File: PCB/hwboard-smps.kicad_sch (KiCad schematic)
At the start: 0 parts

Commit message: add dc dc schematic
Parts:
- added C1, C2, C3, C4, C5, C6, C7, C8: C, symbol Device:C
- added L1: L, symbol Device:L
- added R1, R2, R3, R4, R5: R, symbol Device:R
- added U2: TPS61089, Package_DFN_QFN:Texas_VQFN-RNR0011A-11, symbol Regulator_Switching:TPS61089
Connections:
- new net: R3.2, R4.1, U2.3 (FB)
- new net: R5.1, U2.8 (ILIM)
- new net: C7.1, R2.1, U2.4 (COMP)
- new net: C8.1, R2.2
- new net: C3.1, U2.2 (VCC)
- new net: C1.1, L1.2, R1.1, U2.11 (SW)
- new net: R1.2, U2.1 (FSW)
- new net: C1.2, U2.10 (BOOT)
- new net EN: U2.7 (EN)
- new net GND: C2.2, C3.2, C4.2, C5.2, C6.2, C7.2, C8.2, R4.2, R5.2, U2.5 (GND)
- new net V_{IN}: C2.1, L1.1, U2.9 (VIN)
- new net V_{OUT}: C4.1, C5.1, C6.1, R3.1, U2.6 (VOUT)

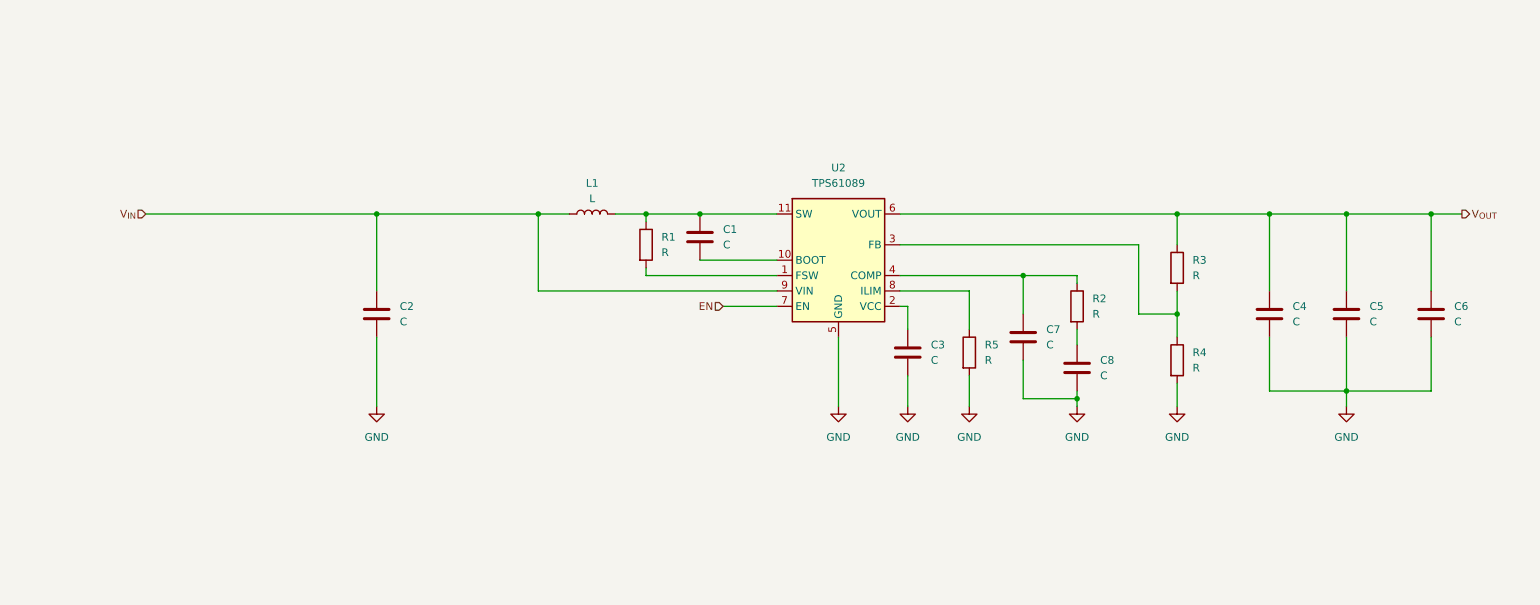
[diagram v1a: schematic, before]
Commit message: add boost components
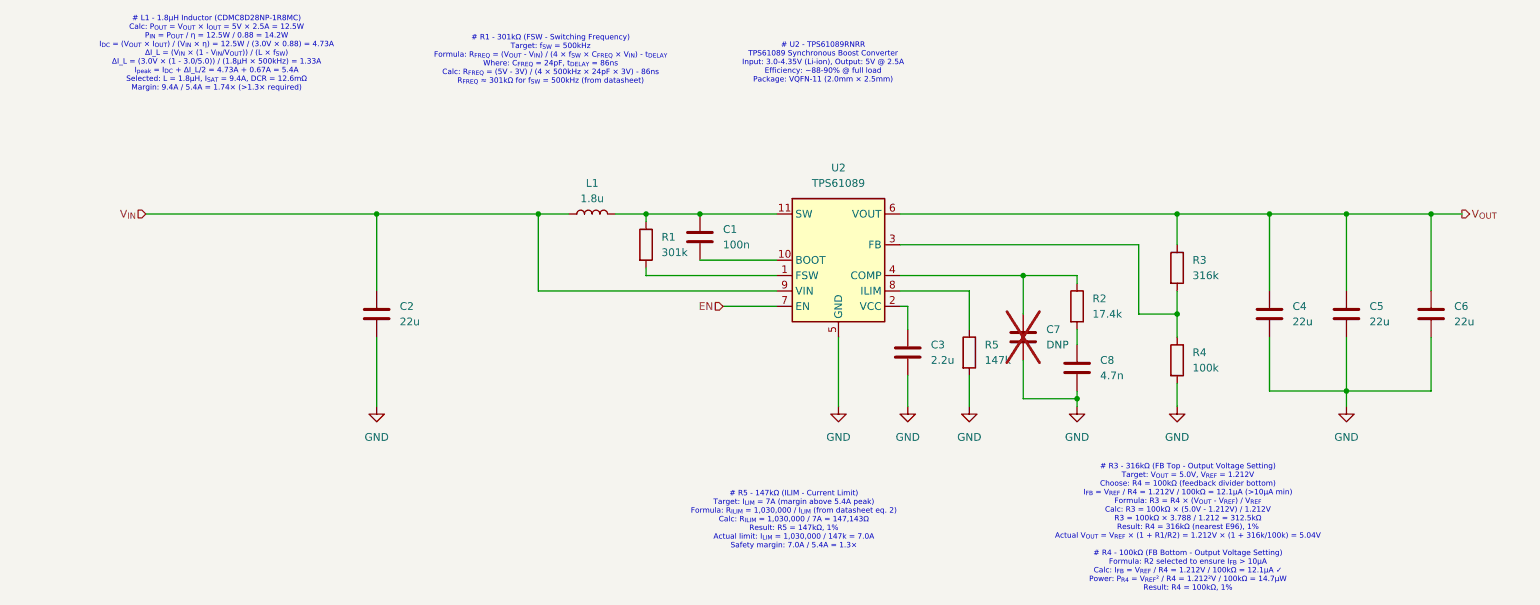
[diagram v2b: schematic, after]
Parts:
- C1: value C -> 100n
- C2, C4, C5, C6: value C -> 22u
- C3: value C -> 2.2u
- C7: value C -> DNP; now not fitted
- C8: value C -> 4.7n
- L1: value L -> 1.8u
- R1: value R -> 301k
- R2: value R -> 17.4k
- R3: value R -> 316k
- R4: value R -> 100k
- R5: value R -> 147k
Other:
- note added: "# L1 - 1.8µH Inductor (CDMC8D28NP-1R8MC) Calc: P_{OUT} = V_{OUT} × I_{OUT} = 5V × 2.5A = 12.5W P_{IN} = P_{OUT} / η = 12.5W / 0.88 = 14.2W I_{DC} = (V_{OUT} × I_{OUT}) / (V_{IN} × η) = 12.5W / (3.0V × 0.88) = 4.73A ΔI_L = (V_{IN} × (1 - V_{IN}/V_{OUT})) / (L × f_{SW}) ΔI_L = (3.0V × (1 - 3.0/5.0)) / (1.8µH × 500kHz) = 1.33A I_{peak} = I_{DC} + ΔI_L/2 = 4.73A + 0.67A = 5.4A Selected: L = 1.8µH, I_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"
- note added: "# R1 - 301kΩ (FSW - Switching Frequency) Target: f_{SW} = 500kHz Formula: R_{FREQ} = (V_{OUT} - V_{IN}) / (4 × f_{SW} × C_{FREQ} × V_{IN}) - t_{DELAY} Where: C_{FREQ} = 24pF, t_{DELAY} = 86ns Calc: R_{FREQ} = (5V - 3V) / (4 × 500kHz × 24pF × 3V) - 86ns R_{FREQ} ≈ 301kΩ for f_{SW} = 500kHz (from datasheet)"
- note added: "# R3 - 316kΩ (FB Top - Output Voltage Setting) Target: V_{OUT} = 5.0V, V_{REF} = 1.212V Choose: R4 = 100kΩ (feedback divider bottom) I_{FB} = V_{REF} / R4 = 1.212V / 100kΩ = 12.1µA (>10µA min) Formula: R3 = R4 × (V_{OUT} - V_{REF}) / V_{REF} Calc: R3 = 100kΩ × (5.0V - 1.212V) / 1.212V R3 = 100kΩ × 3.788 / 1.212 = 312.5kΩ Result: R4 = 316kΩ (nearest E96), 1% Actual V_{OUT} = V_{REF} × (1 + R1/R2) 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"
- note added: "# R5 - 147kΩ (ILIM - Current Limit) Target: I_{LIM} = 7A (margin above 5.4A peak) Formula: R_{ILIM} = 1,030,000 / I_{LIM} (from datasheet eq. 2) Calc: R_{ILIM} = 1,030,000 / 7A = 147,143Ω Result: R5 = 147kΩ, 1% Actual limit: I_{LIM} = 1,030,000 / 147k = 7.0A Safety margin: 7.0A / 5.4A = 1.3×"
- note added: "# U2 - TPS61089RNRR TPS61089 Synchronous Boost Converter Input: 3.0-4.35V (Li-ion), Output: 5V @ 2.5A Efficiency: ~88-90% @ full load Package: VQFN-11 (2.0mm × 2.5mm)"
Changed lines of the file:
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@@
 	(generator_version "9.0")
 	(paper "A4")
+	(text "# U2 - TPS61089RNRR\nTPS61089 Synchronous Boost Converter\nInput: 3.0-4.35V (Li-ion), Output: 5V @ 2.5A\nEfficiency: ~88-90% @ full load\nPackage: VQFN-11 (2.0mm × 2.5mm)"
+		(exclude_from_sim no)
+		(at 148.59 64.008 0)
+		(effects
+			(font
+				(size 0.889 0.889)
+			)
+		)
+	)
+	(text "# R5 - 147kΩ (ILIM - Current Limit)\nTarget: I_{LIM} = 7A (margin above 5.4A peak)\nFormula: R_{ILIM} = 1,030,000 / I_{LIM} (from datasheet eq. 2)\nCalc: R_{ILIM} = 1,030,000 / 7A = 147,143Ω\nResult: R5 = 147kΩ, 1%\nActual limit: I_{LIM} = 1,030,000 / 147k = 7.0A\nSafety margin: 7.0A / 5.4A = 1.3×"
+		(exclude_from_sim no)
+		(at 143.764 139.446 0)
+		(effects
+			(font
+				(size 0.889 0.889)
+			)
+		)
+	)
+	(text "# R1 - 301kΩ (FSW - Switching Frequency)\nTarget: f_{SW} = 500kHz\nFormula: R_{FREQ} = (V_{OUT} - V_{IN}) / (4 × f_{SW} × C_{FREQ} × V_{IN}) - t_{DELAY}\nWhere: C_{FREQ} = 24pF, t_{DELAY} = 86ns\nCalc: R_{FREQ} = (5V - 3V) / (4 × 500kHz × 24pF × 3V) - 86ns\nR_{FREQ} ≈ 301kΩ for f_{SW} = 500kHz (from datasheet)"
+		(exclude_from_sim no)
+		(at 103.632 63.5 0)
+		(effects
+			(font
+				(size 0.889 0.889)
+			)
+		)
+	)
+	(text "# R3 - 316kΩ (FB Top - Output Voltage Setting)\nTarget: V_{OUT} = 5.0V, V_{REF} = 1.212V\nChoose: R4 = 100kΩ (feedback divider bottom)\nI_{FB} = V_{REF} / R4 = 1.212V / 100kΩ = 12.1µA (>10µA min)\nFormula: R3 = R4 × (V_{OUT} - V_{REF}) / V_{REF}\nCalc: R3 = 100kΩ × (5.0V - 1.212V) / 1.212V\nR3 = 100kΩ × 3.788 / 1.212 = 312.5kΩ\nResult: R4 = 316kΩ (nearest E96), 1%\nActual V_{OUT} = V_{REF} × (1 + R1/R2) = 1.212V × (1 + 316k/100k) = 5.04V\n\n# R4 - 100kΩ (FB Bottom - Output Voltage Setting)\nFormula: R2 selected to ensure I_{FB} > 10µA\nCalc: I_{FB} = V_{REF} / R4 = 1.212V / 100kΩ = 12.1µA ✓\nPower: P_{R4} = V_{REF}² / R4 = 1.212²V / 100kΩ = 14.7µW\nResult: R4 = 100kΩ, 1%"
+		(exclude_from_sim no)
+		(at 208.788 140.716 0)
+		(effects
+			(font
+				(size 0.889 0.889)
+			)
+		)
+	)
+	(text "# L1 - 1.8µH Inductor (CDMC8D28NP-1R8MC)\nCalc: P_{OUT} = V_{OUT} × I_{OUT} = 5V × 2.5A = 12.5W\nP_{IN} = P_{OUT} / η = 12.5W / 0.88 = 14.2W\nI_{DC} = (V_{OUT} × I_{OUT}) / (V_{IN} × η) = 12.5W / (3.0V × 0.88) = 4.73A\nΔI_L = (V_{IN} × (1 - V_{IN}/V_{OUT})) / (L × f_{SW})\nΔI_L = (3.0V × (1 - 3.0/5.0)) / (1.8µH × 500kHz) = 1.33A\nI_{peak} = I_{DC} + ΔI_L/2 = 4.73A + 0.67A = 5.4A\nSelected: L = 1.8µH, I_{SAT} = 9.4A, DCR = 12.6mΩ\nMargin: 9.4A / 5.4A = 1.74× (>1.3× required)"
+		(exclude_from_sim no)
+		(at 48.514 62.484 0)
+		(effects
+			(font
+				(size 0.889 0.889)
+			)
+		)
+	)
 	(junction
 		(at 222.25 88.9)
@@
 			)
 		)
-		(property "Value" "R"
+		(property "Value" "316k"
 			(at 209.55 99.0599 0)
 			(effects
@@
 			)
 		)
-		(property "Value" "R"
+		(property "Value" "100k"
 			(at 209.55 114.2999 0)
 			(effects
@@
 			)
 		)
-		(property "Value" "C"
+		(property "Value" "22u"
 			(at 252.73 106.6799 0)
 			(effects
@@
 			)
 		)
-		(property "Value" "C"
+		(property "Value" "22u"
 			(at 78.74 106.6799 0)
 			(effects
@@
 			)
 		)
-		(property "Value" "C"
+		(property "Value" "22u"
 			(at 238.76 106.6799 0)
 			(effects
@@
 			)
 		)
-		(property "Value" "R"
+		(property "Value" "147k"
 			(at 175.26 113.0299 0)
 			(effects
@@
 			)
 		)
-		(property "Value" "R"
+		(property "Value" "17.4k"
 			(at 193.04 105.4099 0)
 			(effects
@@
 			)
 		)
-		(property "Value" "C"
+		(property "Value" "2.2u"
 			(at 166.37 113.0299 0)
 			(effects
@@
 			)
 		)
-		(property "Value" "R"
+		(property "Value" "301k"
 			(at 121.92 95.2499 0)
 			(effects
@@
 		(in_bom yes)
 		(on_board yes)
-		(dnp no)
+		(dnp yes)
 		(fields_autoplaced yes)
 		(property "Reference" "C7"
@@
 			)
 		)
-		(property "Value" "C"
+		(property "Value" "DNP"
 			(at 185.42 110.4899 0)
 			(effects
@@
 			)
 		)
-		(property "Value" "C"
+		(property "Value" "4.7n"
 			(at 194.31 115.5699 0)
 			(effects
@@
 			)
 		)
-		(property "Value" "C"
+		(property "Value" "22u"
 			(at 226.06 106.6799 0)
 			(effects
@@
 			)
 		)
-		(property "Value" "C"
+		(property "Value" "100n"
 			(at 132.08 93.9799 0)
 			(effects
@@
 			)
 		)
-		(property "Value" "L"
+		(property "Value" "1.8u"
 			(at 110.49 86.36 90)
 			(effects
